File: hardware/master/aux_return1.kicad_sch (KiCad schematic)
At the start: 98 parts, among them J201 RETURN 1 L/MONO, J202 RETURN 1 R, J203 GAIN: fitted -6 dB (PRO), ope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, SW201 RETURN 1 MUTE (latching), SW202 RETURN 1 DUCK (latching), SW203 RETURN 1 COMP (latching), U201 AD8273, U202 NE5532, U203 SSI2162, U204 NE5532, U205 NE5532, U206 TL072, U207 TL072, U208 DG413DY, U209 DG413DY

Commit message: Master card: draw decisions 97 and 98, OPA2171 fader-law stages (103), SC_ENV drive (104)
- AUX returns: SC_ENV into the summer's virtual earth through R232/R332 30k1,
  R233/R333 removed, summer + input on AGND (decision 97)
- Q501 emitter and button pull-downs R237/239/241, R337/339/341, R455,
  R523/525/527 to PGND (decision 98)
- U206, U306, U705 = OPA2171 for the pot buffer and control summer; superdiodes
  on the TL072s U207, U307, U706 (decision 103)
- Sidechain: DEPTH negative (R518 to -15 V), U505B follower fed back after R521,
  D504 BAT54T1G clamp to AGND (decision 104); simulation rerun with 1.7 kOhm load
- R421 on its 0603 footprint (system validation finding 3)
- Power budget, parts list, STATUS, decisions and working notes updated

Co-Authored-By: Claude Opus 5.5 <noreply@anthropic.com>
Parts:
- removed R233: 15k8, Resistor_SMD:R_0805_2012Metric, symbol Device:R
- removed U206: TL072, Package_SO:SOIC-8_3.9x4.9mm_P1.27mm, symbol Amplifier_Operational:TL072
- added U206: OPA2171, Package_SO:SOIC-8_3.9x4.9mm_P1.27mm, symbol Amplifier_Operational:Opamp_Dual
- R232: value 100k -> 30k1; Note (none) -> SC_ENV into the virtual earth: 0.332 V/V, 10 dB of ducking 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; ProjectPN SX-R-007 -> SX-R-087
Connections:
- net +15V: now also U206.8 (V+)
- net -15V: now also U206.4 (V-)
- net AGND: now also U206.5 (+); no longer R237.1, R239.1, R241.1
- net PGND: now also R237.1, R239.1, R241.1
- net VC: now also U206.7; no longer U207.7
- net at D201.1 (K): now also U207.7
- net at D201.2 (A), R226.1: now also U207.6 (-)
- net at R222.1, R224.1, R227.1: now also U206.1, U206.2 (-)
- net at R224.2, R225.2: now also U207.5 (+)
- net at C215.1, R222.2, R223.2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: now also R232.2, U206.6 (-); no longer U207.6 (-)
- net at RV201.2: now also U206.3 (+)
- net DUCK_V: now reaches R232.1, U208.2
- removed net VPLUS: R232.2, U207.5 (+)

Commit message: Master card: DRV135 outputs, TL062 levers, SMD electrolytics, both raw rails watched (decisions 125-128)
/board master pre-layout session; the user delegated the open points.
- Confirms the [proposed] parts of decisions 89-94 (Q5 checked, +22 dB
  makeup kept for the breadboard, fallback R439 = 330k).
- 125: TI DRV135UA replaces the end-of-life THAT1646 (THAT memo
  2026-09-01); same SO-8 pinout, LCSC C544663.
- 126: U409, U410, U802, U804 TL072 -> TL062; superdiodes and U407 stay.
- 127: master electrolytics to SMD (decision 111 parts, 5.4 mm).
- 128: U707C watches -20V_RAW (22k6/100k), wired-OR with the +20 V trip.
- Würth fields on J101/J901, BAT54 LCSC C152458, G6K and header
  drawings checked, LCSC stock checked; budget 331/260 mA typical.
- parts.csv candidates for master pots and meter LEDs; lcsc_check.py
  handles MOhm.
ERC 0/0, all netlist checks 0 problems, reuse lint clean.

Co-Authored-By: Claude Opus 5.5 <noreply@anthropic.com>
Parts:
- C205, C206, C209, C210: footprint Capacitor_THT:C_Radial_D5.0mm_H11.0mm_P2.00mm -> Capacitor_SMD:C_Elec_6.3x5.4; MPN (none) -> EEE-1VA100NP; Manufacturer (none) -> Panasonic; ProjectPN SX-C-003 -> SX-C-023; Supplier (none) -> Mouser; SupplierPN (none) -> 667-EEE-1VA100NP

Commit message: System: cost review and cost control (decisions 132-137)
Rean NYS216 jacks with a new footprint (132), through-hole parts hand-soldered (133), E24 values owned per board (134), live-device cost principle (135), /cost with the cost-controller sub-agent, tools/costs.py and a private ledger of realized costs (136), JLCPCB fee-free parts first (137).

Co-Authored-By: Claude Opus 5.5 <noreply@anthropic.com>
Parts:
- J201, J202: footprint Connector_Audio:Jack_6.35mm_Neutrik_NMJ6HCD2_Horizontal -> syntsamix:Jack_6.35mm_Rean_NYS216_Horizontal; MPN NMJ6HCD2 -> NYS216; Manufacturer Neutrik -> Rean; ProjectPN SX-CONN-001 -> SX-CONN-015
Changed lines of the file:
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@@
 			)
 		)
-		(property "Footprint" "Connector_Audio:Jack_6.35mm_Neutrik_NMJ6HCD2_Horizontal"
+		(property "Footprint" "syntsamix:Jack_6.35mm_Rean_NYS216_Horizontal"
 			(at 30.48 50.8 0)
 			(hide yes)
@@
 			)
 		)
-		(property "ProjectPN" "SX-CONN-001"
+		(property "ProjectPN" "SX-CONN-015"
 			(at 30.48 50.8 0)
 			(hide yes)
@@
 			)
 		)
-		(property "Manufacturer" "Neutrik"
+		(property "Manufacturer" "Rean"
 			(at 30.48 50.8 0)
 			(hide yes)
@@
 			)
 		)
-		(property "MPN" "NMJ6HCD2"
+		(property "MPN" "NYS216"
 			(at 30.48 50.8 0)
 			(hide yes)
@@
 			)
 		)
-		(property "Footprint" "Connector_Audio:Jack_6.35mm_Neutrik_NMJ6HCD2_Horizontal"
+		(property "Footprint" "syntsamix:Jack_6.35mm_Rean_NYS216_Horizontal"
 			(at 30.48 76.2 0)
 			(hide yes)
@@
 			)
 		)
-		(property "ProjectPN" "SX-CONN-001"
+		(property "ProjectPN" "SX-CONN-015"
 			(at 30.48 76.2 0)
 			(hide yes)
@@
 			)
 		)
-		(property "Manufacturer" "Neutrik"
+		(property "Manufacturer" "Rean"
 			(at 30.48 76.2 0)
 			(hide yes)
@@
 			)
 		)
-		(property "MPN" "NMJ6HCD2"
+		(property "MPN" "NYS216"
 			(at 30.48 76.2 0)
 			(hide yes)

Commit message: Master card: fee-free parts and E24 values (decisions 144, 146-150)
- 144: AUX return and master fader laws on the channel's E24 pairs
- 146: meter ladder on fee-free E24 values (0.45 mA, within 0.14 dB); R732 22k + R737 560R
- 147: compressor R420/R426 E24 pairs, GR LED ladder 470k/4k3, SC LPF C503 2 x 47n C0G
  (Q 0.707, 44-478 Hz); TL072 symbols ST TL072CDT
- 148: AUX return receivers TL072 difference amplifiers (AD8273 gone from the project)
- 149: R421 plain 1k; compressor temperature compensation to the backlog
- 150: DG413, SSI2162, DRV135UA, AS3046D hand-soldered on the prototype master
  (symbol field Assembly, read by tools/costs.py); SPOF noted in the backlog
- Part swaps: button LEDs per colour, D504 BAT54W, D705-D712 1N4007W SOD-123FL,
  U641 DG411 -> DG413 with a Q601 inverter for send 1 (emitter on PGND, invariant 4)
- 70 -> 38 extended/consigned SMD types (about EUR 193 -> 105 per order);
  estimate EUR 794 / 1,074 / 1,671 for 4 / 8 / 16 channels
- Docs: STATUS, CONTINUE-FROM-HERE, ROADMAP backlog, SPEC, hardware/CLAUDE.md lessons

Co-Authored-By: Claude Opus 5.5 <noreply@anthropic.com>
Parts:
- removed U201: AD8273, Package_SO:SOIC-14_3.9x8.7mm_P1.27mm, symbol syntsamix:AD8273
- added R242: 13k, Resistor_SMD:R_0805_2012Metric, symbol Device:R
- added R243: 150k, Resistor_SMD:R_0805_2012Metric, symbol Device:R
- added R244: 24k, Resistor_SMD:R_0805_2012Metric, symbol Device:R
- added R245, R246, R247, R248, R249, R250, R251, R252: 10k, Resistor_SMD:R_0805_2012Metric, symbol Device:R
- added U201: TL072, Package_SO:SOIC-8_3.9x4.9mm_P1.27mm, symbol Amplifier_Operational:TL072
- D203: MPN (none) -> NCD0805R1; Manufacturer (none) -> Foshan NationStar; ProjectPN SX-D-002 -> SX-D-015; Supplier (none) -> LCSC; SupplierPN (none) -> C84256
- D204, D205: MPN (none) -> KT-0805G; Manufacturer (none) -> Hubei KENTO; ProjectPN SX-D-002 -> SX-D-011; Supplier (none) -> LCSC; SupplierPN (none) -> C2297
- R201, R202, R203, R204: value 100 -> 10k; MPN (none) -> RT0805BRD0710KL; Manufacturer (none) -> YAGEO; Note (none) -> 0.1 %: receiver resistor match sets the CMRR (decision 148); ProjectPN SX-R-001 -> SX-R-107; Supplier (none) -> LCSC; SupplierPN (none) -> C110775
- R222: value 113k -> 100k; ProjectPN SX-R-023 -> SX-R-007
- R223: value 453k -> 300k; ProjectPN SX-R-024 -> SX-R-096
- R225: value 221k -> 220k; ProjectPN SX-R-025 -> SX-R-103
- R226: value 63k4 -> 62k; ProjectPN SX-R-026 -> SX-R-102
- R228: value 124k -> 100k; ProjectPN SX-R-027 -> SX-R-007
- R229: value 8k66 -> 9k1; ProjectPN SX-R-014 -> SX-R-095
- R231: value 33k2 -> 33k; ProjectPN SX-R-028 -> SX-R-006
- U203, U208, U209: Assembly (none) -> hand (decision 150)
- U207: MPN (none) -> TL072CDT; Manufacturer Texas Instruments -> STMicroelectronics; Supplier (none) -> LCSC; SupplierPN (none) -> C6961
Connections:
- net +15V: now also R244.1, U201.8 (V+); no longer R228.1
- net -15V: now also U201.4 (V-)
- net AGND: now also R248.1, R252.1
- net at C206.1: now also R250.2, U201.7
- net at C205.1: now also R246.2, U201.1
- net at C201.1, R201.2: now also R245.1
- net at C202.1, R202.2: now also R247.1
- net at C204.1, R204.2: now also R251.1
- net at C203.1, R203.2: now also R249.1
- net at C215.1, R226.2, R229.2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: now also R242.2, R243.2; no longer R222.2, R223.2
- new net: R249.2, R250.1, U201.6 (-)
- new net: R222.2, R242.1
- new net: R228.1, R244.2
- new net: R251.2, R252.2, U201.5 (+)
- new net: R223.2, R243.1
- new net: R245.2, R246.1, U201.2 (-)
- new net: R247.2, R248.2, U201.3 (+)
- no-connect marks 12 -> 10

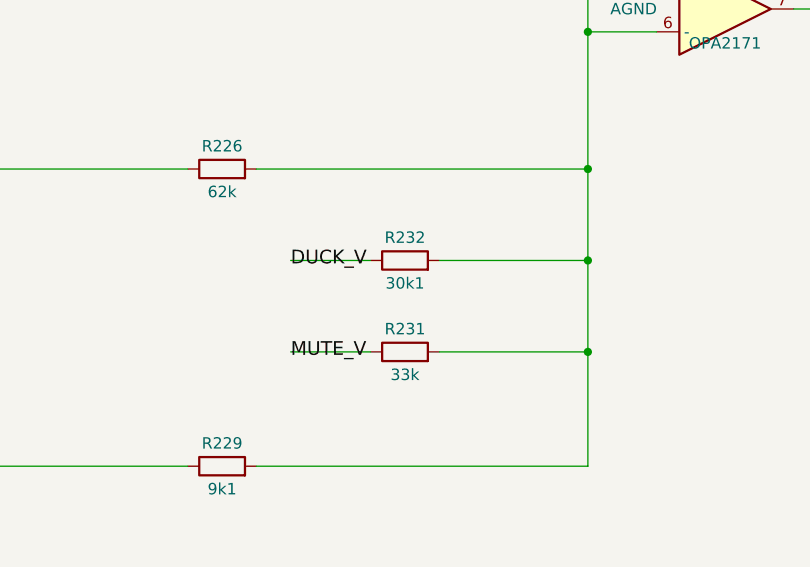
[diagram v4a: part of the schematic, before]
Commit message: Master card: R232/R332 30k (decision 153)
AUX return sheets: R232/R332 30k1 -> 30k (SX-R-050, JLCPCB basic);
SX-R-087 no longer used. simulation/sidechain load 18 x 30k = 1.667 kOhm,
results unchanged. Netlists match (73 nets each), ERC 0/0. Cost: 35 fee
types, EUR 785/1,066/1,663 for 4/8/16 channels. STATUS.md trimmed;
drawn part swaps moved to CHECKLISTS.md.

Co-Authored-By: Claude Opus 5.5 <noreply@anthropic.com>
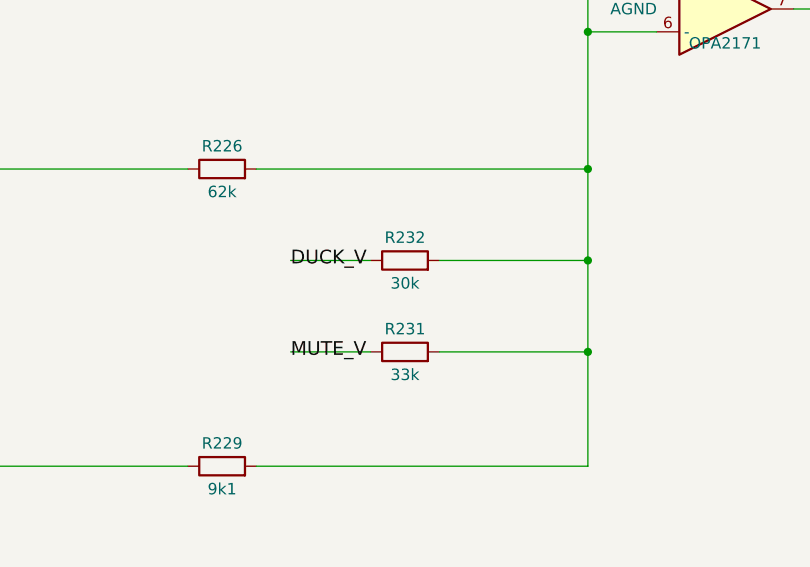
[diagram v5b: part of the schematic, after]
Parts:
- R232: value 30k1 -> 30k; Note SC_ENV into the virtual earth: 0.332 V/V, 10 dB of ducking 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 -> SC_ENV into the virtual earth: 0.333 V/V, 10 dB of ducking 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; ProjectPN SX-R-087 -> SX-R-050

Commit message: Buttons: SX-SW-001 is the latching GPBS850L, not the momentary GPBS850N
Electrokit 41012905 (on-on, latching) links the GPBS850N datasheet, which
is the momentary twin (Electrokit 41015527, Mouser "Non-Latching ON-(ON)");
the MPN was copied from that file. The latching part is CW GPBS850L
(datasheet Rev 2, 2014: same body, pin grid and pressed = 2-3, 5-6 contacts;
plunger 4.0 mm instead of 3.8).

MPN and footprint name corrected on all 17 button symbols, the generator
scripts and the input reference; parts.csv gets the GPBS850L datasheet and
RoHS source (Mouser 629-GPBS-850L, DigiKey CW179-ND); prices.csv gets the
Electrokit price (6.48 SEK ex VAT at 25+). Erratum on decision 75, checklist
item for the delivered switches and cap sizing, correction notes in the
RoHS audit and the cost review. No wiring change; ERC 0/0 on both cards.
Estimate €769 / €1,037 / €1,609 for 4 / 8 / 16 channels.

Co-Authored-By: Claude Opus 5.5 <noreply@anthropic.com>
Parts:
- SW201, SW202, SW203: footprint syntsamix:SW_Latching_8.5x8.5mm_CW_GPBS850N -> syntsamix:SW_Latching_8.5x8.5mm_CW_GPBS850L; MPN GPBS850N -> GPBS850L
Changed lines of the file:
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@@
 			)
 		)
-		(property "Footprint" "syntsamix:SW_Latching_8.5x8.5mm_CW_GPBS850N"
+		(property "Footprint" "syntsamix:SW_Latching_8.5x8.5mm_CW_GPBS850L"
 			(at 421.64 289.56 0)
 			(hide yes)
@@
 			)
 		)
-		(property "MPN" "GPBS850N"
+		(property "MPN" "GPBS850L"
 			(at 421.64 289.56 0)
 			(hide yes)
@@
 			)
 		)
-		(property "Footprint" "syntsamix:SW_Latching_8.5x8.5mm_CW_GPBS850N"
+		(property "Footprint" "syntsamix:SW_Latching_8.5x8.5mm_CW_GPBS850L"
 			(at 421.64 320.04 0)
 			(hide yes)
@@
 			)
 		)
-		(property "MPN" "GPBS850N"
+		(property "MPN" "GPBS850L"
 			(at 421.64 320.04 0)
 			(hide yes)
@@
 			)
 		)
-		(property "Footprint" "syntsamix:SW_Latching_8.5x8.5mm_CW_GPBS850N"
+		(property "Footprint" "syntsamix:SW_Latching_8.5x8.5mm_CW_GPBS850L"
 			(at 421.64 350.52 0)
 			(hide yes)
@@
 			)
 		)
-		(property "MPN" "GPBS850N"
+		(property "MPN" "GPBS850L"
 			(at 421.64 350.52 0)
 			(hide yes)

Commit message: Master: rear jacks on two 26-pin row-board ribbons (decision 163)
J603 (AUX sends sheet) carries main outs and both AUX sends to the
output row board; J903 (Power sheet) brings the AUX returns, SC EXT
and the ground-lift switch (pins 25/26) from the input row board.
Pairs with a ground between them; row boards hold only jacks, header
and SW901. Netlist checks 0 problems, ERC 0/0.

Co-Authored-By: Claude Opus 5.5 <noreply@anthropic.com>
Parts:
- removed J201: RETURN 1 L/MONO, syntsamix:Jack_6.35mm_Rean_NYS216_Horizontal, symbol Connector_Audio:AudioJack3_Switch
- removed J202: RETURN 1 R, syntsamix:Jack_6.35mm_Rean_NYS216_Horizontal, symbol Connector_Audio:AudioJack3_Switch
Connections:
- net IN_L+ renamed RET1_L+
- net IN_L- renamed RET1_L-
- net IN_R+ renamed RET1_R+
- net IN_R- renamed RET1_R-
- no-connect marks 10 -> 6

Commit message: Master: back-to-back coupling pairs, ten NE5532 to TL072, Wakefield heatsinks, onsemi TO-220 regulators (decisions 172-174)
Co-Authored-By: Claude Opus 5.5 <noreply@anthropic.com>
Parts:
- removed C205, C206, C209, C210: 10u bipolar, Capacitor_SMD:C_Elec_6.3x5.4, symbol Device:C
- removed U202, U204, U205: NE5532, Package_SO:SOIC-8_3.9x4.9mm_P1.27mm, symbol Amplifier_Operational:NE5532
- added C205, C206, C209, C210, C234, C235, C236, C237: 10u 35V, Capacitor_SMD:CP_Elec_5x5.4, symbol Device:C_Polarized
- added U202, U204, U205: TL072, Package_SO:SOIC-8_3.9x4.9mm_P1.27mm, symbol Amplifier_Operational:TL072
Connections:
- net +15V: now also U202.8 (V+), U204.8 (V+), U205.8 (V+)
- net -15V: now also U202.4 (V-), U204.4 (V-), U205.4 (V-)
- net AGND: now also U202.3 (+), U202.5 (+), U204.3 (+), U204.5 (+), U205.3 (+), U205.5 (+)
- net R_RET: now also C210.1, U202.7
- net at C213.2, R215.2, R217.1: now also U204.1
- net at C213.1, R215.1, U203.4 (IOUT1): now also U204.2 (-)
- net at C207.2, J203.2 (Pin_2), R209.2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: now also C209.1, U202.1
- net at C208.1, R206.2, R208.1: now also U202.6 (-)
- net at R250.2, U201.7: now also C206.1
- net at R218.2, R220.1: now also U205.6 (-)
- net at R220.2, R235.1: now also U205.7
- net at C214.1, R216.1, U203.7 (IOUT2): now also U204.6 (-)
- net at C214.2, R216.2, R218.1: now also U204.7
- net at R217.2, R219.1: now also U205.2 (-)
- net at R219.2, R234.1: now also U205.1
- net at R211.1: now also C236.1
- net at R246.2, U201.1: now also C205.1
- net at R206.1: now also C235.1
- net at C207.1, R205.2, R207.1: now also U202.2 (-)
- net at R205.1: now also C234.1
- net at R212.1: now also C237.1
- new net: C210.2, C237.2
- new net: C209.2, C236.2
- new net: C206.2, C235.2
- new net: C205.2, C234.2
